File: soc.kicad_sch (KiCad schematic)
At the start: 12 parts, among them J3 Conn_ARM_SWD_TagConnect_TC203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, U1 MDBT50Q-512K, U3 LSM6DSOXTR, U4 MAX30102, Y1 Crystal

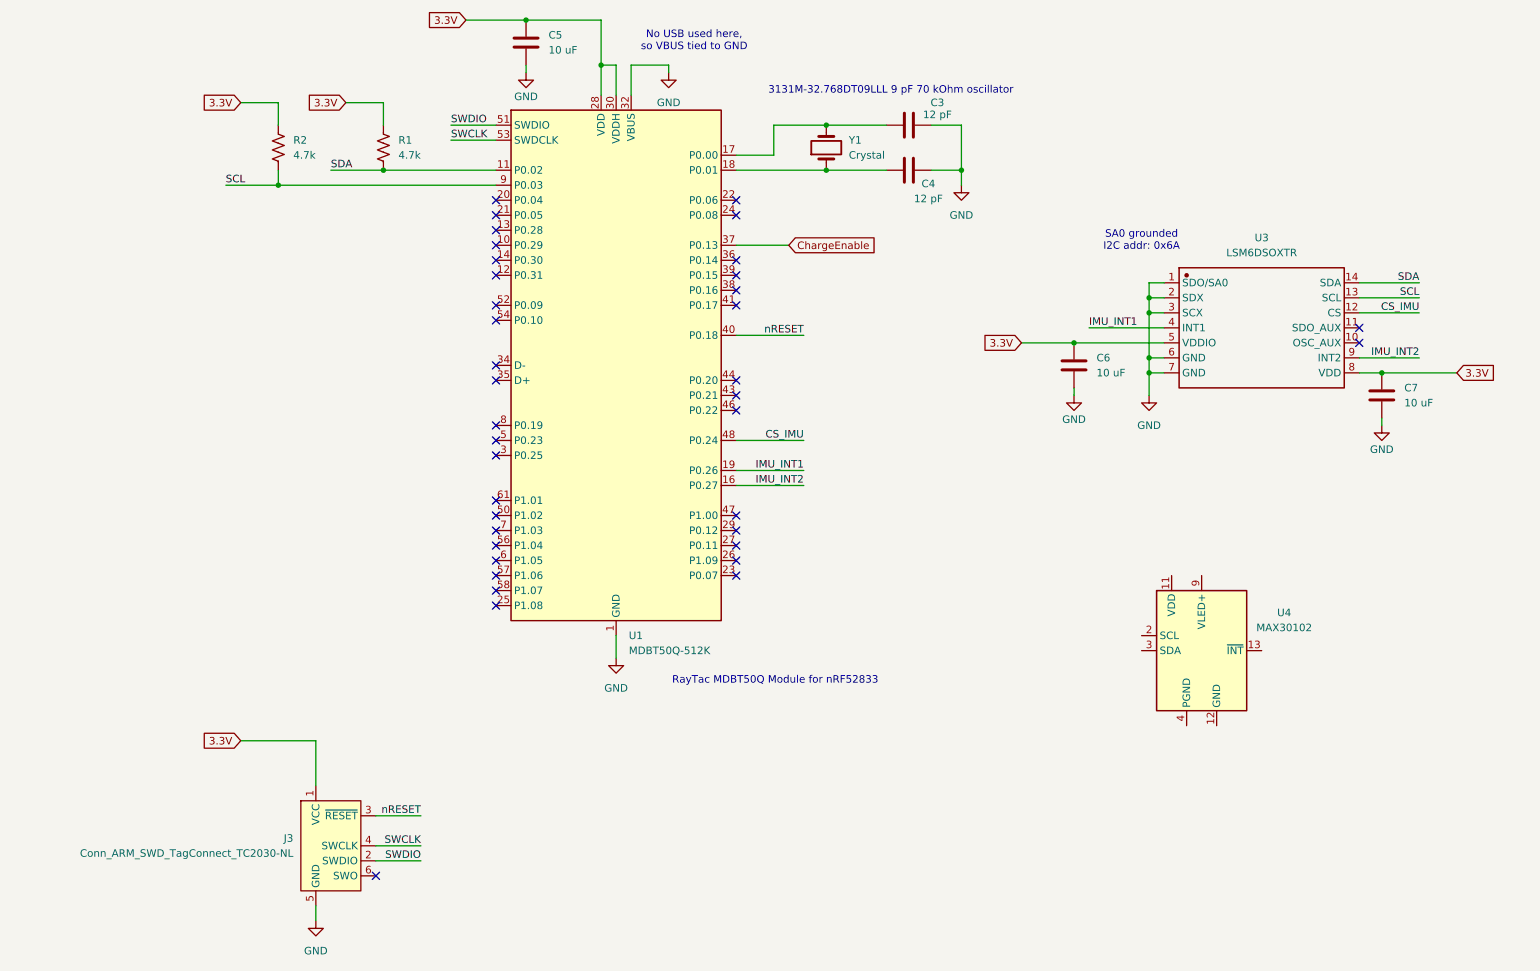
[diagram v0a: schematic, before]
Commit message: update to include footprints from project specific lib
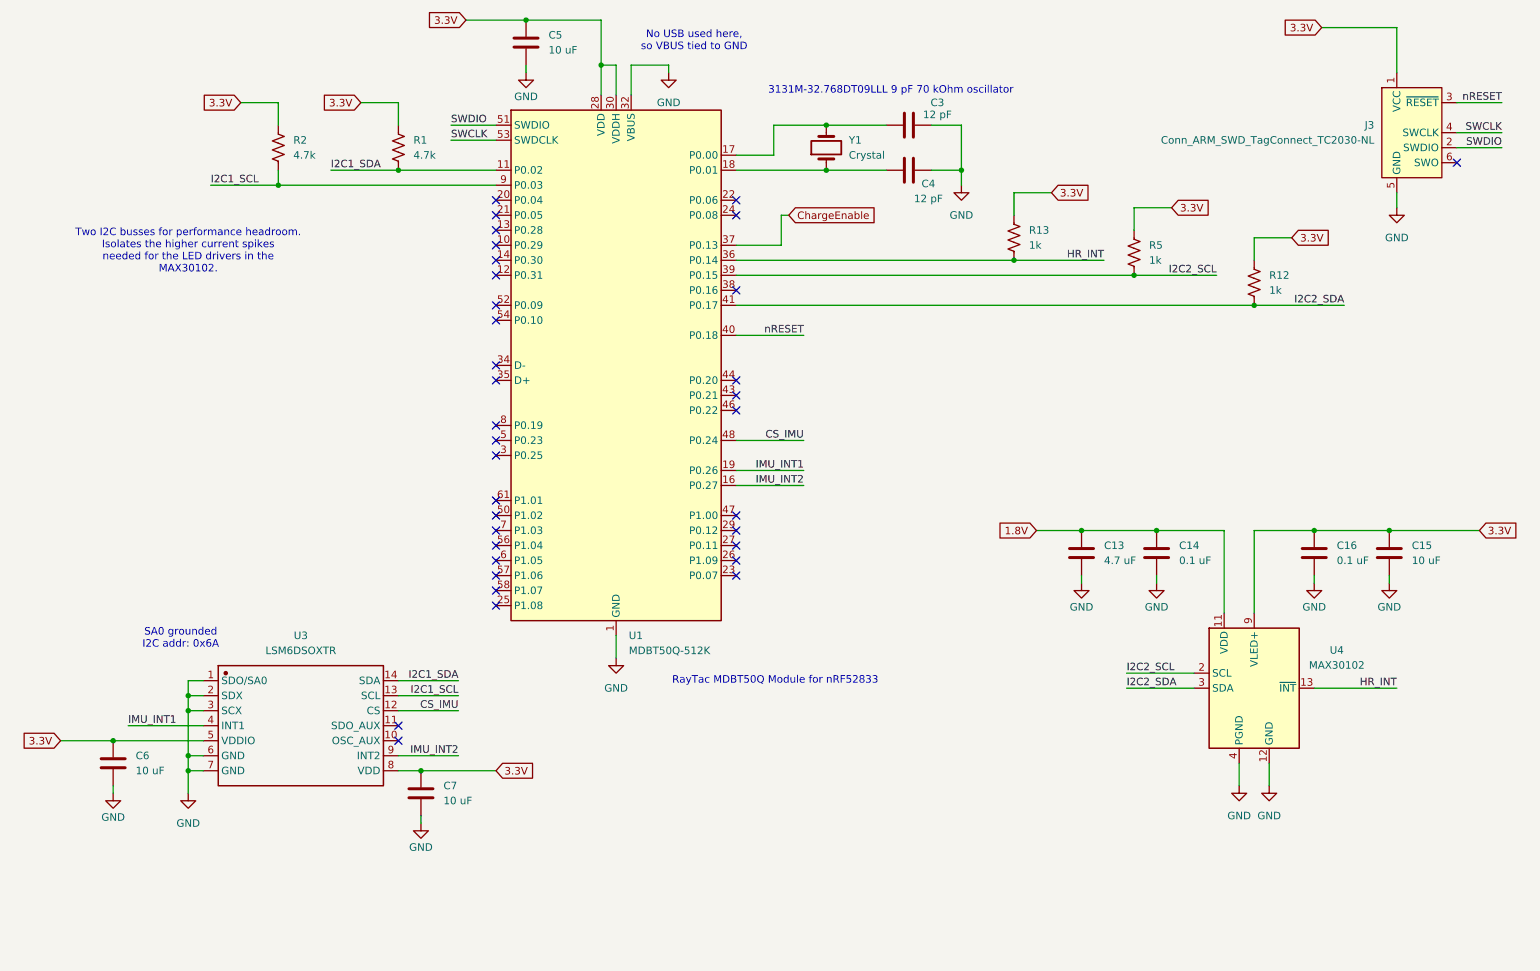
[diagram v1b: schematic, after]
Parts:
- added C13: 4.7 uF, PCM_JLCPCB:C_0402, symbol Device:C
- added C14, C16: 0.1 uF, PCM_JLCPCB:C_0402, symbol Device:C
- added C15: 10 uF, PCM_JLCPCB:C_0402, symbol Device:C
- added R12, R13, R5: 1k, PCM_JLCPCB:R_0402, symbol Device:R_US
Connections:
- net 3.3V: now also U4.10 (VLED+), U4.9 (VLED+), C15.1, C16.2, R12.1, R13.1, R5.1
- net GND: now also U4.12 (GND), U4.4 (PGND), C13.2, C14.2, C15.2, C16.1
- net 1.8V: now reaches U4.11 (VDD)
- net 1.8V: now also C13.1, C14.1
- net HR_INT: now reaches U4.13 (~{INT})
- net HR_INT: now also U1.36 (P0.14), R13.2
- net I2C2_SCL: now reaches U4.2 (SCL)
- net I2C2_SCL: now also U1.39 (P0.15), R5.2
- net I2C2_SDA: now reaches U4.3 (SDA)
- net I2C2_SDA: now also U1.41 (P0.17), R12.2
- net SCL renamed I2C1_SCL
- net SDA renamed I2C1_SDA
- no-connect marks 38 -> 35
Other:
- note added: "Two I2C busses for performance headroom. Isolates the higher current spikes needed for the LED drivers in the MAX30102."
- moved on the sheet: C6, C7, J3, R1, U3, U4
